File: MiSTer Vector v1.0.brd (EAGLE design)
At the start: 63 x 63.9 mm, 35 parts, among them CON2 22-23-2021, IC2 TL084, IC3 TL084, IC7 MAX6105, U1 MCP4922, U2 MCP4922, U3 MCP4922, U8 VASD1-SIP

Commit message: hook up DE15 pins 6,7,8 to Gnd
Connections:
- net GND: now also J1.6, J1.7, J1.8
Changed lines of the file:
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@@
 <contactref element="IC2" pad="10"/>
 <contactref element="CON2" pad="2"/>
+<contactref element="J1" pad="6"/>
+<contactref element="J1" pad="7"/>
+<contactref element="J1" pad="8"/>
+<wire x1="68.58" y1="-9.784" x2="68.58" y2="-7.494" width="0" layer="19" extent="1-1"/>
+<wire x1="68.58" y1="-12.074" x2="68.58" y2="-9.784" width="0" layer="19" extent="1-1"/>
+<wire x1="68.58" y1="-16.654" x2="68.58" y2="-12.074" width="0" layer="19" extent="1-1"/>
 </signal>
 <signal name="DACR">

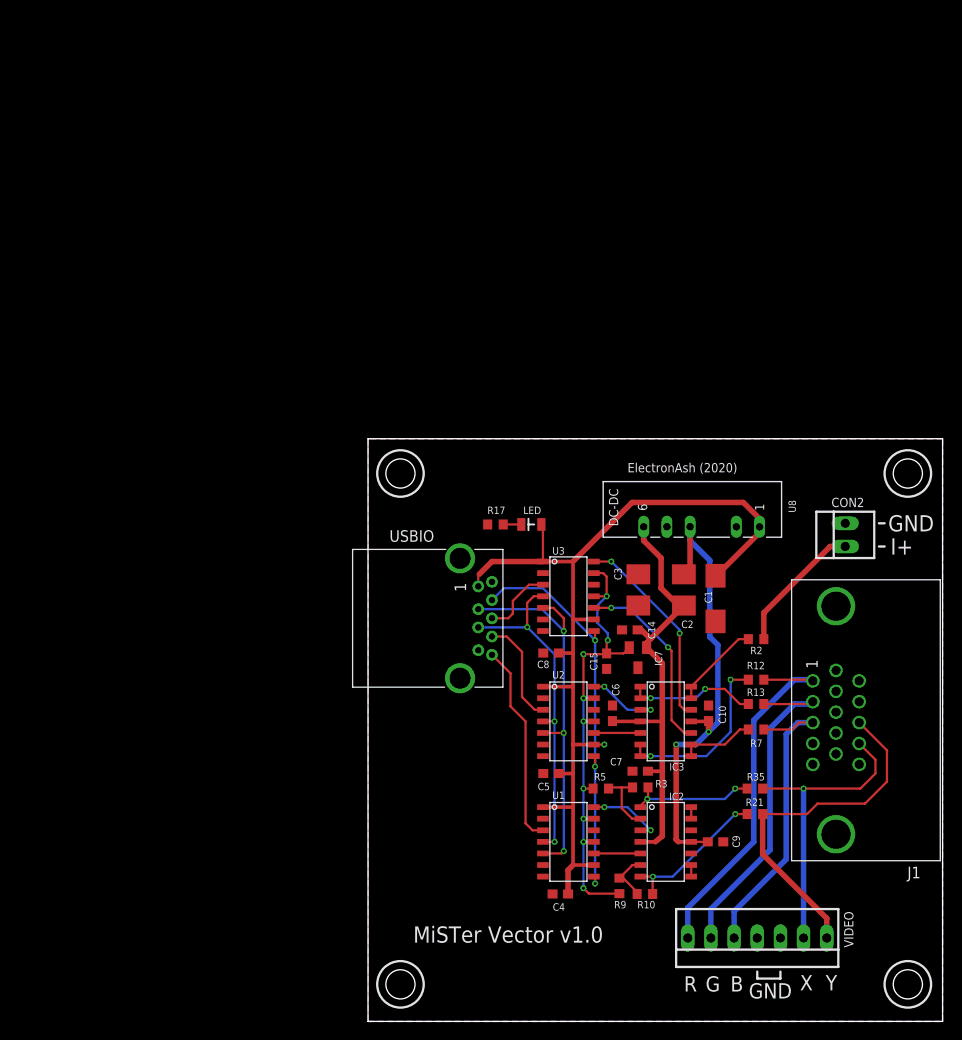
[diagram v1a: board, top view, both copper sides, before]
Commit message: driving the DAC chips in parallel now, because FPGAs rule
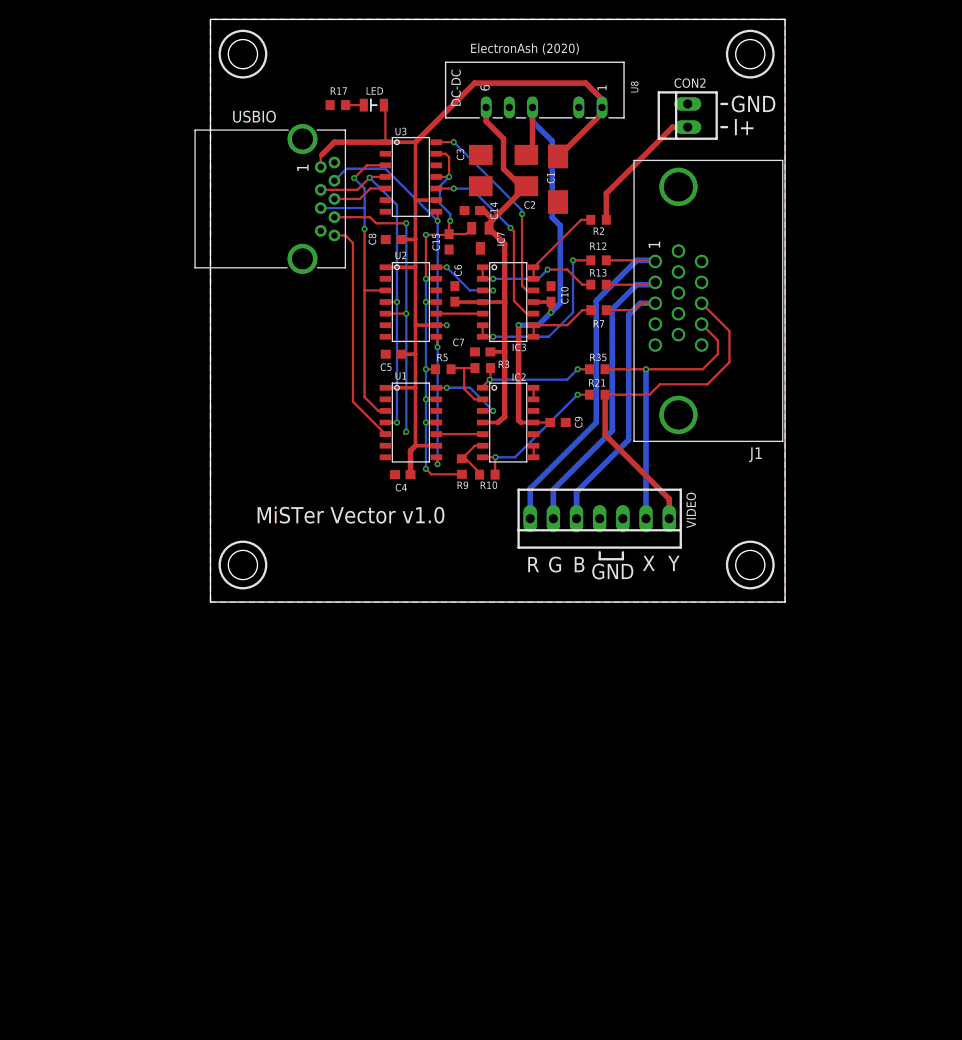
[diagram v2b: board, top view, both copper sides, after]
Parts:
- moved C5 49.1 mm to (20.1, 27.2)
- moved CON2 49.1 mm to (52.3, 53.3)
- moved C1 49.1 mm to (38.1, 46.4)
- moved C10 49.1 mm to (37.3, 33.8)
- moved C14 49.1 mm to (28.7, 42.9)
- moved C15 49.1 mm to (26.2, 39.5)
- moved C2 49.1 mm to (32.1, 45.6)
- moved C3 49.1 mm to (32.1, 49.0)
- moved C4 49.1 mm to (21.1, 14.0)
- moved C6 49.1 mm to (26.8, 33.8)
- moved C7 49.1 mm to (29.8, 27.4)
- moved C9 49.1 mm to (38.1, 19.7)
- moved IC2 49.1 mm to (30.6, 24.0)
- moved IC3 49.1 mm to (30.6, 37.2)
- moved IC7 49.1 mm to (29.6, 39.9)
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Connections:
- removed net DAC_CS_BI_N: U3.3, USBIO.7
- removed net DAC_CS_RG_N: U2.3, USBIO.6
- removed net DAC_CS_XY_N: U1.3, USBIO.5
- removed net SPI_DAT: U1.5, U2.5, U3.5, USBIO.2
- new net DAC_BI_DAT: U3.5, USBIO.7
- new net DAC_CS_N: U1.3, U2.3, U3.3, USBIO.3
- new net DAC_RG_DAT: U2.5, USBIO.6
- new net DAC_XY_DAT: U1.5, USBIO.5
- net SPI_CLK: now also USBIO.2; no longer USBIO.3
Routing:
- net SPI_DAT: track 43.3 -> 0.00 mm, vias 3 -> 0
- net DAC_CS_N: track 0.00 -> 38.5 mm, vias 0 -> 2
- net DAC_RG_DAT: track 0.00 -> 33.7 mm, vias 0 -> 3
- net DAC_XY_DAT: track 0.00 -> 24.8 mm
- net DAC_CS_XY_N: track 22.2 -> 0.00 mm
- net DAC_CS_RG_N: track 11.8 -> 0.00 mm
- net DAC_CS_BI_N: track 7.93 -> 0.00 mm
- net DAC_BI_DAT: track 0.00 -> 6.06 mm
- net SPI_CLK: track 37.4 -> 38.3 mm

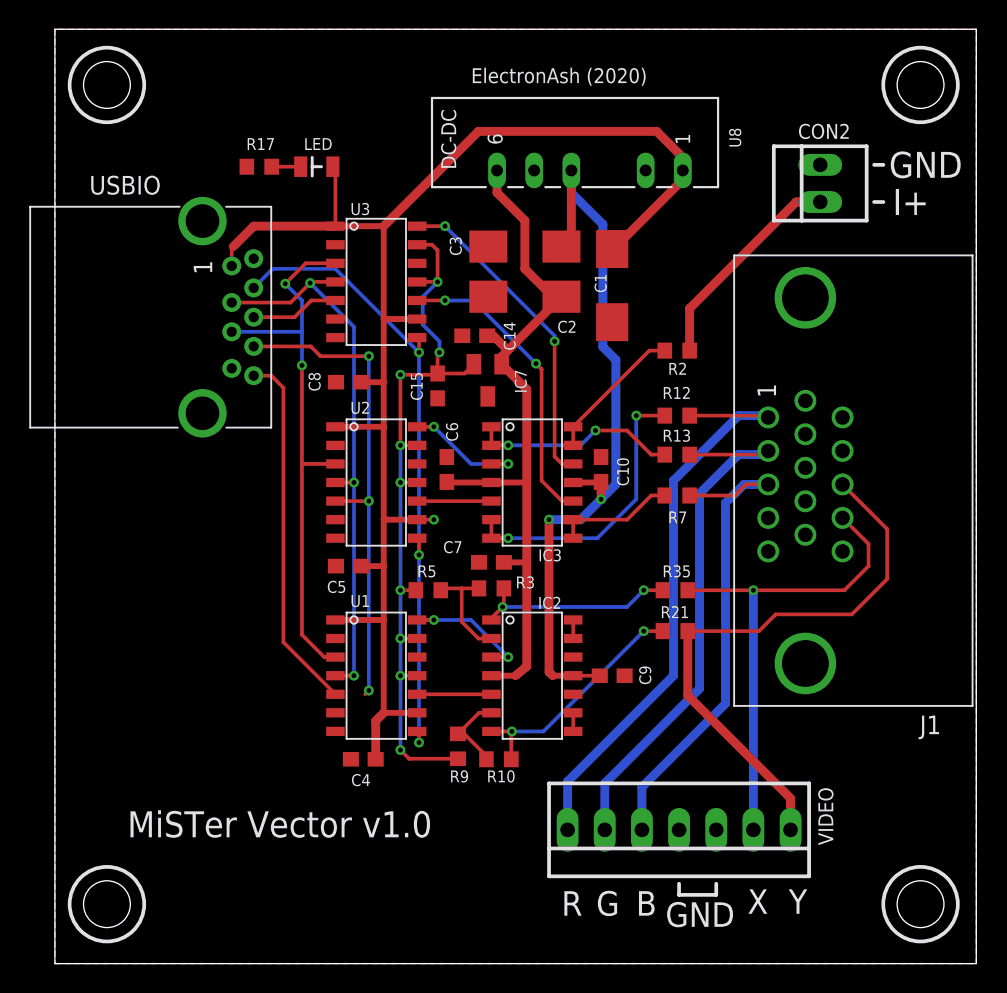
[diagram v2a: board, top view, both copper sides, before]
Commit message: added 3-pin VESA miniDIN, for 3D glasses
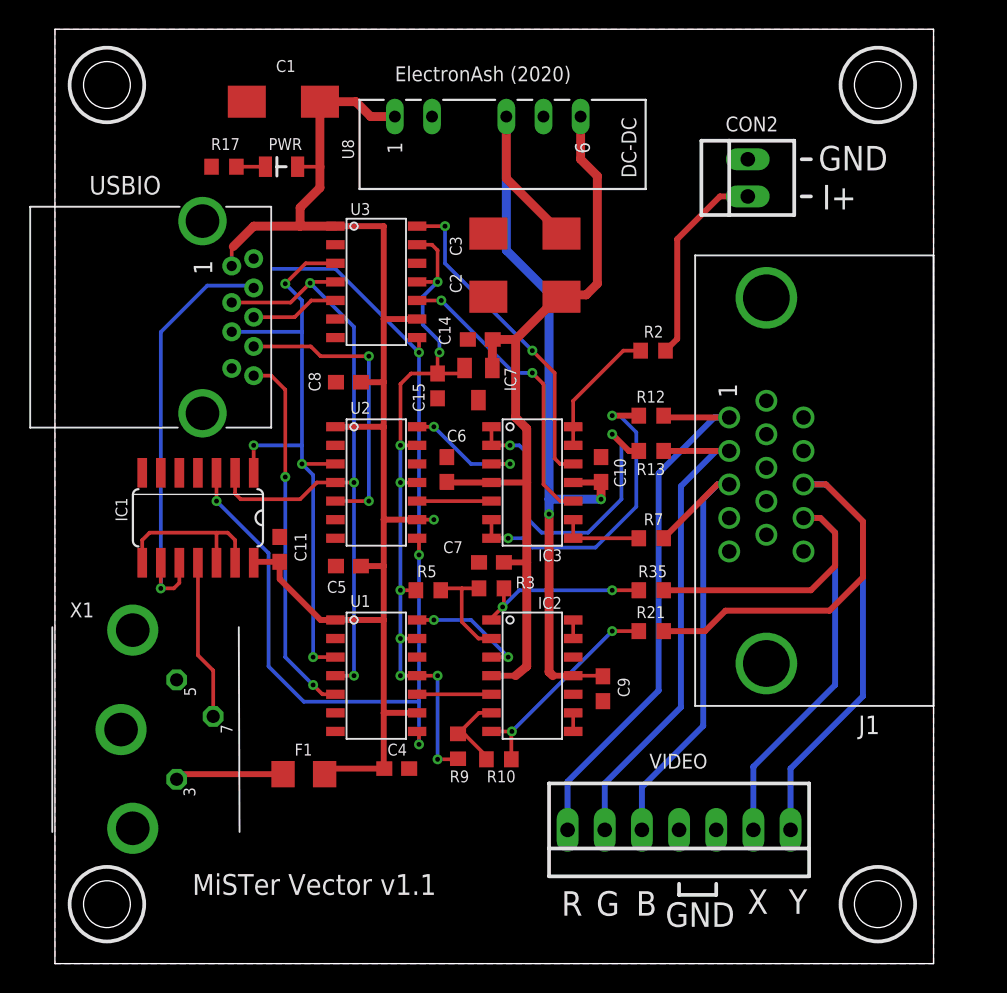
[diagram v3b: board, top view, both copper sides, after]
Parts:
- removed LED: SD_LED, dan-led:0805_POL
- added C11: 0.1uF, adafruit:C0603
- added F1: 100mA, adafruit:R1206
- added IC1: 74HC00D, 74xx-eu:SO14
- added PWR: SD_LED, dan-led:0805_POL
- added X1: (no value), mini_din:M_DIN3
- moved C1 25.8 mm to (15.6, 58.9), turned to 180 degrees
- moved U8 7.90 mm to (29.6, 57.9), turned to 90 degrees
- moved CON2 4.97 mm to (47.4, 53.7)
- moved R7 3.42 mm to (40.8, 29.1)
- moved J1 2.67 mm to (48.6, 33.0)
- moved R17 2.41 mm to (11.6, 54.5)
- moved C4 2.37 mm to (23.4, 13.3), turned to 0 degrees
- moved R13 1.80 mm to (40.8, 35.1)
- moved R12 1.78 mm to (40.8, 37.5)
- moved R2 1.65 mm to (40.9, 41.9)
- moved R21 1.65 mm to (40.8, 22.7)
- moved R35 1.65 mm to (40.8, 25.5)
- moved C9 1.09 mm to (37.5, 18.8), turned to 90 degrees
- moved C3 0.89 mm to (32.1, 49.9)
- moved IC7 0.68 mm to (29.0, 39.6)
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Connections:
- removed net DAC_LDAC_N: U1.8, U2.8, U3.8, USBIO.8
- new net 3D_SYNC_TTL: IC1.11, X1.7
- new net 3D_SYNC_USBIO: IC1.10, IC1.9, USBIO.8
- new net DAC_LAT_N: IC1.3, U1.8, U2.8, U3.8
- new net N$6: F1.1, X1.3
- new net N$8: IC1.12, IC1.13, IC1.8
- net +5V: now also C11.1, F1.2, IC1.14, PWR.+; no longer LED.+
- net DAC_CS_N: now also IC1.1
- net GND: now also C11.2, IC1.4, IC1.5, IC1.7, X1.5, X1.SH1, X1.SH2, X1.SH3
- net N$10: now also PWR.-; no longer LED.-
- net SPI_CLK: now also IC1.2
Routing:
- net DAC_LAT_N: track 0.00 -> 68.6 mm, vias 0 -> 4
- net DAC_LDAC_N: track 44.2 -> 0.00 mm, vias 3 -> 0
- net 3D_SYNC_USBIO: track 0.00 -> 29.8 mm, vias 0 -> 1
- net DAC_RG_DAT: track 33.7 -> 20.3 mm, vias 3 -> 2
- net Y+: track 39.3 -> 52.3 mm
- net N$8: track 0.00 -> 11.9 mm
- net 3D_SYNC_TTL: track 0.00 -> 10.9 mm
- net X+: track 33.5 -> 42.5 mm, vias 1 -> 0
- net G1+: track 14.2 -> 23.2 mm
- net SPI_CLK: track 38.3 -> 47.2 mm
- net -12V: track 50.9 -> 59.2 mm
- net +5V: track 103.4 -> 95.4 mm
- net N$6: track 0.00 -> 7.42 mm
- net +12V: track 50.0 -> 55.8 mm
- net DAC_CS_N: track 38.5 -> 44.1 mm, vias 2 -> 4
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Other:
- board size 63 x 63.9 mm -> 60.1 x 63.9 mm
- board text added: "MiSTer Vector v1.1"
- board text removed: "MiSTer Vector v1.0"

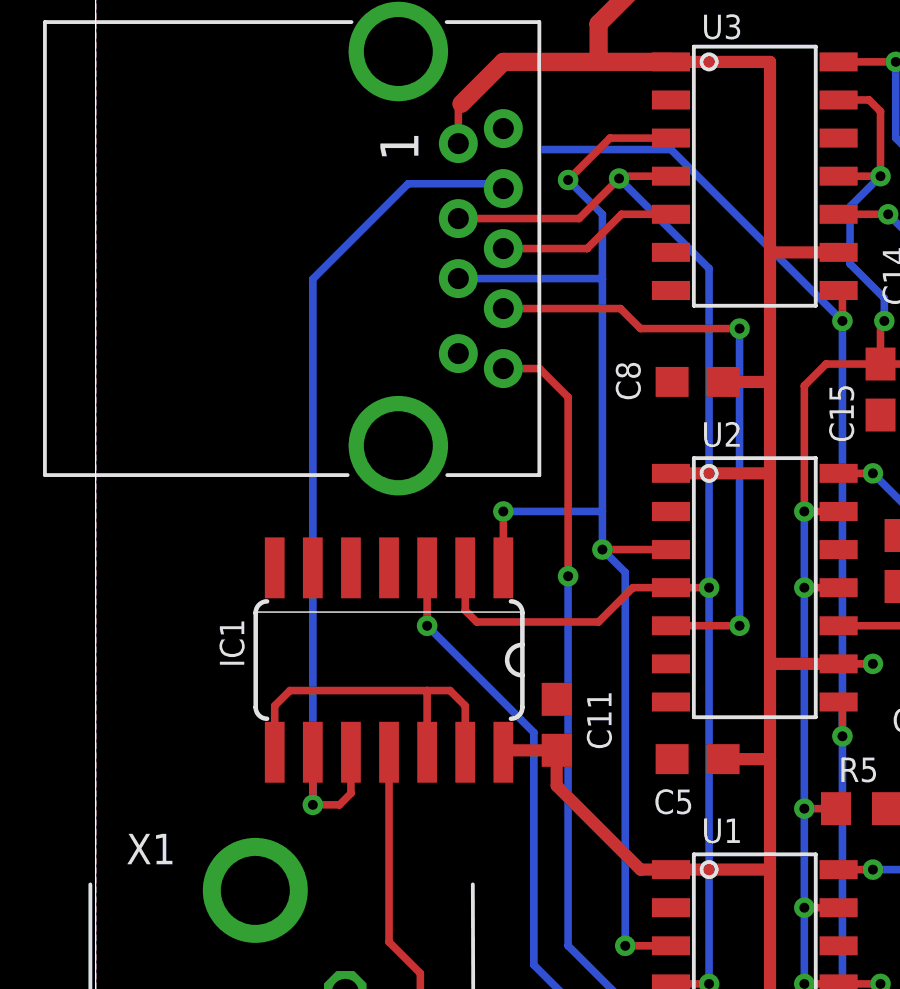
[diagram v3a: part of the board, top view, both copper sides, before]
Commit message: swapped two USBIO pins, for better signal integrity
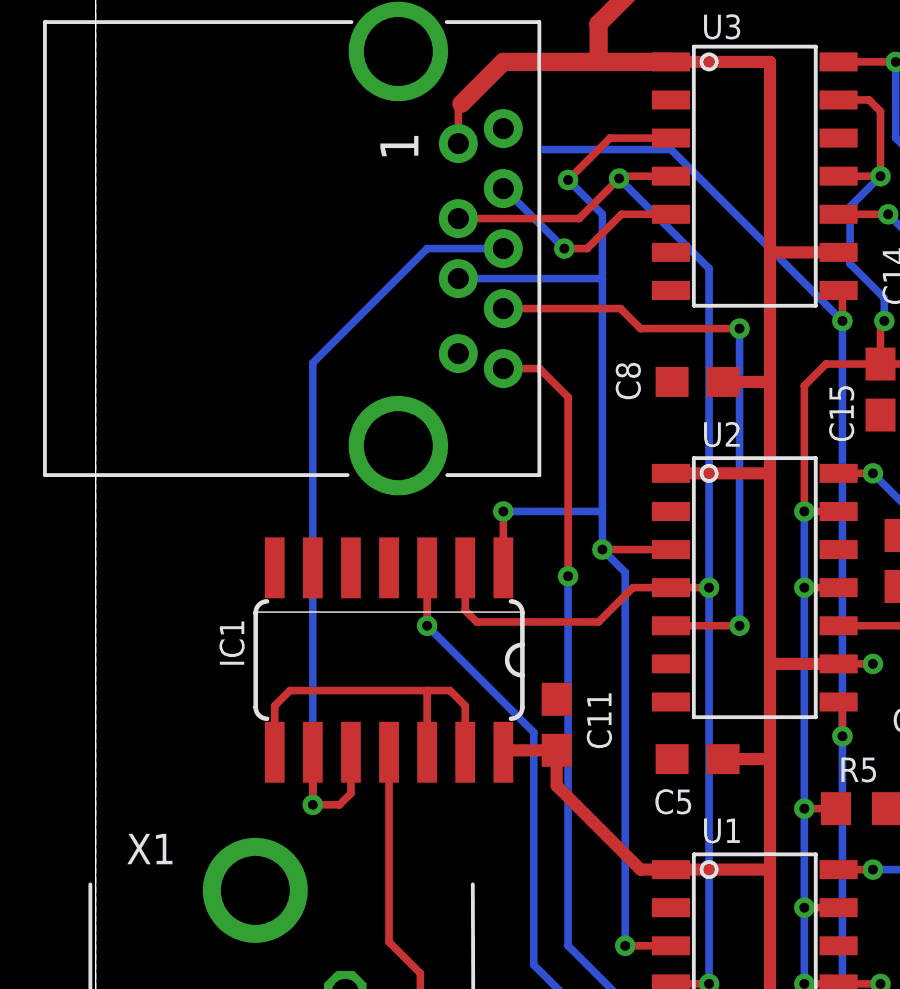
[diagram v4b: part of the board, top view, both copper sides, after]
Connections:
- net 3D_SYNC_USBIO: now also USBIO.7; no longer USBIO.8
- net DAC_BI_DAT: now also USBIO.8; no longer USBIO.7
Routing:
- net 3D_SYNC_USBIO: track 29.8 -> 27.2 mm
- net DAC_BI_DAT: track 6.06 -> 6.89 mm, vias 0 -> 1
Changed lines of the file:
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@@
 <signal name="DAC_BI_DAT">
 <contactref element="U3" pad="5"/>
-<contactref element="USBIO" pad="7"/>
-<wire x1="13.589" y1="44.196" x2="16.383" y2="44.196" width="0.254" layer="1"/>
 <wire x1="16.383" y1="44.196" x2="17.526" y2="45.339" width="0.254" layer="1"/>
 <wire x1="17.526" y1="45.339" x2="19.177" y2="45.339" width="0.254" layer="1"/>
+<contactref element="USBIO" pad="8"/>
+<wire x1="16.383" y1="44.196" x2="15.621" y2="44.196" width="0.254" layer="1"/>
+<via x="15.621" y="44.196" extent="1-16" drill="0.3302"/>
+<wire x1="15.621" y1="44.196" x2="13.621" y2="46.196" width="0.254" layer="16"/>
+<wire x1="13.621" y1="46.196" x2="13.589" y2="46.196" width="0.254" layer="16"/>
 </signal>
 <signal name="DAC_XY_DAT">
@@
 </signal>
 <signal name="3D_SYNC_USBIO">
-<contactref element="USBIO" pad="8"/>
 <contactref element="IC1" pad="9"/>
 <contactref element="IC1" pad="10"/>
-<wire x1="13.589" y1="46.196" x2="13.43" y2="46.355" width="0.254" layer="16"/>
-<wire x1="13.43" y1="46.355" x2="10.414" y2="46.355" width="0.254" layer="16"/>
-<wire x1="10.414" y1="46.355" x2="7.239" y2="43.18" width="0.254" layer="16"/>
-<wire x1="7.239" y1="43.18" x2="7.239" y2="25.654" width="0.254" layer="16"/>
 <via x="7.239" y="25.654" extent="1-16" drill="0.3302"/>
 <wire x1="7.239" y1="25.654" x2="7.239" y2="27.4066" width="0.254" layer="1"/>
@@
 <wire x1="8.509" y1="26.035" x2="8.128" y2="25.654" width="0.254" layer="1"/>
 <wire x1="8.128" y1="25.654" x2="7.239" y2="25.654" width="0.254" layer="1"/>
+<contactref element="USBIO" pad="7"/>
+<wire x1="7.239" y1="25.654" x2="7.239" y2="40.386" width="0.254" layer="16"/>
+<wire x1="7.239" y1="40.386" x2="11.049" y2="44.196" width="0.254" layer="16"/>
+<wire x1="11.049" y1="44.196" x2="13.589" y2="44.196" width="0.254" layer="16"/>
 </signal>
 <signal name="N$8">
